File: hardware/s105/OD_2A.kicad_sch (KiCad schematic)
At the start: 10 parts, among them Q1 BC847C

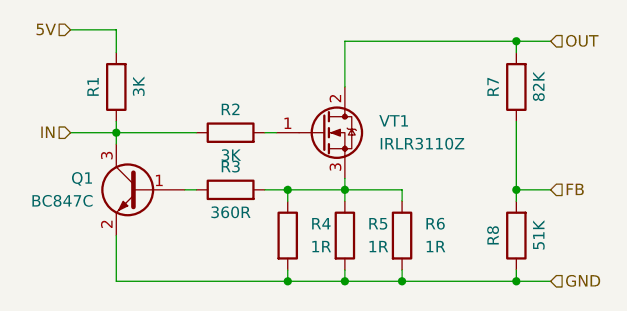
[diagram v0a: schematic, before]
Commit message: разместила схожие блоки
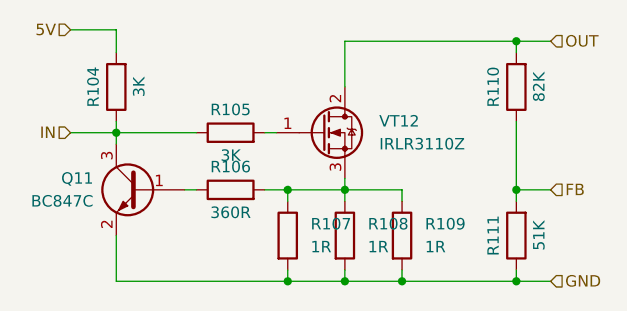
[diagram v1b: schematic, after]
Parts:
- renumbered Q1 to Q11, R1 to R104, R2 to R105, R3 to R106, R4 to R107, R5 to R108, R6 to R109, R7 to R110, R8 to R111, VT1 to VT12
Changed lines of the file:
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@@
   (symbol (lib_id "Device:R") (at 161.29 86.36 0) (unit 1)
     (in_bom yes) (on_board yes) (fields_autoplaced)
-    (property "Reference" "R5" (id 0) (at 163.83 85.0899 0)
+    (property "Reference" "R108" (id 0) (at 163.83 85.0899 0)
       (effects (font (size 1.27 1.27)) (justify left))
     )
@@
   (symbol (lib_id "Transistor_FET:IRFS4115") (at 158.75 74.93 0) (unit 1)
     (in_bom yes) (on_board yes) (fields_autoplaced)
-    (property "Reference" "VT1" (id 0) (at 165.1 73.6599 0)
+    (property "Reference" "VT12" (id 0) (at 165.1 73.6599 0)
       (effects (font (size 1.27 1.27)) (justify left))
     )
@@
   (symbol (lib_id "Transistor_BJT:BC847") (at 138.43 81.28 0) (mirror y) (unit 1)
     (in_bom yes) (on_board yes) (fields_autoplaced)
-    (property "Reference" "Q1" (id 0) (at 133.35 80.0099 0)
+    (property "Reference" "Q11" (id 0) (at 133.35 80.0099 0)
       (effects (font (size 1.27 1.27)) (justify left))
     )
@@
   (symbol (lib_id "Device:R") (at 148.59 74.93 90) (unit 1)
     (in_bom yes) (on_board yes)
-    (property "Reference" "R2" (id 0) (at 148.59 72.39 90))
+    (property "Reference" "R105" (id 0) (at 148.59 72.39 90))
     (property "Value" "3K" (id 1) (at 148.59 77.47 90))
     (property "Footprint" "Resistor_SMD:R_0603_1608Metric" (id 2) (at 148.59 76.708 90)
@@
   (symbol (lib_id "Device:R") (at 180.34 86.36 180) (unit 1)
     (in_bom yes) (on_board yes)
-    (property "Reference" "R8" (id 0) (at 177.8 86.36 90))
+    (property "Reference" "R111" (id 0) (at 177.8 86.36 90))
     (property "Value" "51K" (id 1) (at 182.88 86.36 90))
     (property "Footprint" "Resistor_SMD:R_0603_1608Metric" (id 2) (at 182.118 86.36 90)
@@
   (symbol (lib_id "Device:R") (at 135.89 69.85 180) (unit 1)
     (in_bom yes) (on_board yes)
-    (property "Reference" "R1" (id 0) (at 133.35 69.85 90))
+    (property "Reference" "R104" (id 0) (at 133.35 69.85 90))
     (property "Value" "3K" (id 1) (at 138.43 69.85 90))
     (property "Footprint" "Resistor_SMD:R_0603_1608Metric" (id 2) (at 137.668 69.85 90)
@@
   (symbol (lib_id "Device:R") (at 154.94 86.36 0) (unit 1)
     (in_bom yes) (on_board yes) (fields_autoplaced)
-    (property "Reference" "R4" (id 0) (at 157.48 85.0899 0)
+    (property "Reference" "R107" (id 0) (at 157.48 85.0899 0)
       (effects (font (size 1.27 1.27)) (justify left))
     )
@@
   (symbol (lib_id "Device:R") (at 148.59 81.28 90) (unit 1)
     (in_bom yes) (on_board yes)
-    (property "Reference" "R3" (id 0) (at 148.59 78.74 90))
+    (property "Reference" "R106" (id 0) (at 148.59 78.74 90))
     (property "Value" "360R" (id 1) (at 148.59 83.82 90))
     (property "Footprint" "Resistor_SMD:R_0603_1608Metric" (id 2) (at 148.59 83.058 90)
@@
   (symbol (lib_id "Device:R") (at 180.34 69.85 180) (unit 1)
     (in_bom yes) (on_board yes)
-    (property "Reference" "R7" (id 0) (at 177.8 69.85 90))
+    (property "Reference" "R110" (id 0) (at 177.8 69.85 90))
     (property "Value" "82K" (id 1) (at 182.88 69.85 90))
     (property "Footprint" "Resistor_SMD:R_0805_2012Metric" (id 2) (at 182.118 69.85 90)
@@
   (symbol (lib_id "Device:R") (at 167.64 86.36 0) (unit 1)
     (in_bom yes) (on_board yes) (fields_autoplaced)
-    (property "Reference" "R6" (id 0) (at 170.18 85.0899 0)
+    (property "Reference" "R109" (id 0) (at 170.18 85.0899 0)
       (effects (font (size 1.27 1.27)) (justify left))
     )
